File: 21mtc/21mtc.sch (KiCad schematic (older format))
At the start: 4 parts, among them P101 CONN_01X11, P102 CONN_02X11, P103 CONN_01X11, P104 CONN_02X04

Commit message: Layout of a first draft
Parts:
- removed P101: CONN_01X11, symbol CONN_01X10
- added P101: CONN_01X06, Connectors:solderpads_1x06_2mm, symbol CONN_01X06
- added P105: CONN_01X04, Connectors:solderpads_1x04_2mm, symbol CONN_01X04
- P102: footprint (none) -> Connectors:Pin_Header_Straight_2x11_1.27_smd
- P103: footprint (none) -> Connectors:solderpads_1x11_2mm
- P104: footprint (none) -> Pin_Headers:Pin_Header_Straight_2x04
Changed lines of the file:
@@
 F 0 "P102" H 4650 3800 50  0000 C CNN
 F 1 "CONN_02X11" V 4650 3200 50  0000 C CNN
-F 2 "" H 4650 2000 60  0000 C CNN
+F 2 "Connectors:Pin_Header_Straight_2x11_1.27_smd" H 4650 2000 60  0001 C CNN
 F 3 "" H 4650 2000 60  0000 C CNN
 	1    4650 3200
@@
 F 0 "P103" H 5400 2600 50  0000 C CNN
 F 1 "CONN_01X11" V 5500 3200 50  0000 C CNN
-F 2 "" H 5400 3200 60  0000 C CNN
+F 2 "Connectors:solderpads_1x11_2mm" H 5400 3200 60  0001 C CNN
 F 3 "" H 5400 3200 60  0000 C CNN
 F 4 "Value" H 5400 3200 60  0001 C CNN "Fieldname"
 	1    5400 3200
 	1    0    0    1
-$EndComp
-$Comp
-L CONN_01X10 P101
-U 1 1 566E68DE
-P 3900 3150
-F 0 "P101" H 3900 3700 50  0000 C CNN
-F 1 "CONN_01X11" V 4000 3150 50  0000 C CNN
-F 2 "" H 3900 3150 60  0000 C CNN
-F 3 "" H 3900 3150 60  0000 C CNN
-F 4 "Value" H 3900 3150 60  0001 C CNN "Fieldname"
-	1    3900 3150
-	-1   0    0    -1
 $EndComp
 Wire Wire Line
@@
 F 0 "P104" H 7100 3300 50  0000 C CNN
 F 1 "CONN_02X04" H 7100 2800 50  0000 C CNN
-F 2 "" H 7100 1850 60  0000 C CNN
+F 2 "Pin_Headers:Pin_Header_Straight_2x04" H 7100 1850 60  0001 C CNN
 F 3 "" H 7100 1850 60  0000 C CNN
 	1    7100 3050
@@
 Text Notes 7700 4000 2    60   ~ 0
 NEM 652 / NMRA Medium
+$Comp
+L CONN_01X06 P101
+U 1 1 566EB905
+P 3900 2950
+F 0 "P101" H 3900 3300 50  0000 C CNN
+F 1 "CONN_01X06" V 4000 2950 50  0000 C CNN
+F 2 "Connectors:solderpads_1x06_2mm" H 3900 2950 60  0001 C CNN
+F 3 "" H 3900 2950 60  0000 C CNN
+	1    3900 2950
+	-1   0    0    -1
+$EndComp
+$Comp
+L CONN_01X04 P105
+U 1 1 566EB947
+P 3900 3450
+F 0 "P105" H 3900 3200 50  0000 C CNN
+F 1 "CONN_01X04" V 4000 3450 50  0000 C CNN
+F 2 "Connectors:solderpads_1x04_2mm" H 3900 3450 60  0001 C CNN
+F 3 "" H 3900 3450 60  0000 C CNN
+	1    3900 3450
+	-1   0    0    -1
+$EndComp
 $EndSCHEMATC

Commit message: MTC21 Updates
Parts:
- added Q101: NTJD4401N, Housings_SOT-23_SOT-143_TSOT-6:SC-70-6_Handsoldering, symbol NTJD4401N
- added R101, R102, R103, R104: R, Resistors_SMD:R_0805_HandSoldering, symbol R
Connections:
- net GND: now also Q101.1 (S), Q101.4 (S), R101.2, R104.2
- net Aux3: no longer names the net of P103.2 (P2)
- net Aux3: now also Q101.3 (D); no longer P102.20 (P20)
- net Aux4: no longer names the net of P101.4 (P4)
- net Aux4: now also Q101.6 (D); no longer P102.7 (P7)
- new net: Q101.5 (G), R103.1, R104.1
- new net: Q101.2 (G), R101.1, R102.2
- new net Aux3_ttl: P102.20 (P20), R103.2
- new net Aux4_ttl: P102.7 (P7), R102.1
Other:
- moved on the sheet: P103
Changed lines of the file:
@@
 EESchema Schematic File Version 2
+LIBS:21mtc-rescue
 LIBS:power
 LIBS:device
@@
 LIBS:valves
 LIBS:21mtclogo
+LIBS:NTJD4401N
 LIBS:21mtc-cache
 EELAYER 25 0
@@
 L CONN_01X11 P103
 U 1 1 566E68B8
-P 5400 3200
-F 0 "P103" H 5400 2600 50  0000 C CNN
-F 1 "CONN_01X11" V 5500 3200 50  0000 C CNN
-F 2 "Connectors:solderpads_1x11_2mm" H 5400 3200 60  0001 C CNN
-F 3 "" H 5400 3200 60  0000 C CNN
-F 4 "Value" H 5400 3200 60  0001 C CNN "Fieldname"
-	1    5400 3200
+P 5800 3200
+F 0 "P103" H 5800 2600 50  0000 C CNN
+F 1 "CONN_01X11" V 5900 3200 50  0000 C CNN
+F 2 "Connectors:solderpads_1x11_2mm" H 5800 3200 60  0001 C CNN
+F 3 "" H 5800 3200 60  0000 C CNN
+F 4 "Value" H 5800 3200 60  0001 C CNN "Fieldname"
+	1    5800 3200
 	1    0    0    1
 $EndComp
@@
 	4100 2900 4400 2900
 Wire Wire Line
-	4100 3000 4400 3000
-Wire Wire Line
 	4100 3100 4400 3100
 Wire Wire Line
@@
 	4400 3600 4100 3600
 Wire Wire Line
-	4900 2700 5200 2700
-Wire Wire Line
-	5200 2800 4900 2800
-Wire Wire Line
-	4900 2900 5200 2900
-Wire Wire Line
-	5200 3000 4900 3000
-Wire Wire Line
-	4900 3100 5200 3100
-Wire Wire Line
-	4900 3200 5200 3200
-Wire Wire Line
-	5200 3300 4900 3300
-Wire Wire Line
-	4900 3400 5200 3400
-Wire Wire Line
-	5200 3500 4900 3500
-Wire Wire Line
-	4900 3600 5200 3600
-Wire Wire Line
-	5200 3700 4900 3700
+	4900 2700 5600 2700
+Wire Wire Line
+	4900 2800 5600 2800
+Wire Wire Line
+	4900 2900 5600 2900
+Wire Wire Line
+	4900 3000 5600 3000
+Wire Wire Line
+	4900 3100 5600 3100
+Wire Wire Line
+	4900 3200 5600 3200
+Wire Wire Line
+	4900 3300 5600 3300
+Wire Wire Line
+	4900 3400 5600 3400
+Wire Wire Line
+	4900 3500 5600 3500
+Wire Wire Line
+	4900 3700 5600 3700
 Text Label 4100 2700 0    60   ~ 0
 Hall1
@@
 Text Label 4100 2900 0    60   ~ 0
 Hall3
-Text Label 4100 3000 0    60   ~ 0
-Aux4
+Text Label 4400 3000 2    60   ~ 0
+Aux4_ttl
 Text Label 4100 3100 0    60   ~ 0
 TBClock
@@
 Vcc
 Text Label 4900 3600 0    60   ~ 0
-Aux3
+Aux3_ttl
 Text Label 4900 3500 0    60   ~ 0
 Aux2
@@
 L LOGO #G101
 U 1 1 566E6F08
-P 4650 4650
-F 0 "#G101" H 4650 4104 60  0001 C CNN
-F 1 "LOGO" H 4650 5196 60  0001 C CNN
-F 2 "" H 4650 4650 60  0000 C CNN
-F 3 "" H 4650 4650 60  0000 C CNN
-	1    4650 4650
-	1    0    0    -1
-$EndComp
-Text Notes 3900 4000 0    60   ~ 0
+P 4650 5100
+F 0 "#G101" H 4650 4554 60  0001 C CNN
+F 1 "LOGO" H 4650 5646 60  0001 C CNN
+F 2 "" H 4650 5100 60  0000 C CNN
+F 3 "" H 4650 5100 60  0000 C CNN
+	1    4650 5100
+	1    0    0    -1
+$EndComp
+Text Notes 3900 4450 0    60   ~ 0
 Tries to follow NMRA S9.1.1
 $Comp
@@
 	-1   0    0    -1
 $EndComp
+Wire Wire Line
+	4900 3600 5000 3600
+Wire Wire Line
+	4400 3000 4300 3000
+$Comp
+L NTJD4401N Q101
+U 2 1 56717E2C
+P 5400 4050
+F 0 "Q101" H 5600 4125 50  0000 L CNN
+F 1 "NTJD4401N" H 5600 4050 50  0000 L CNN
+F 2 "Housings_SOT-23_SOT-143_TSOT-6:SC-70-6_Handsoldering" H 5600 3975 50  0000 L CIN
+F 3 "" H 5400 4050 50  0000 L CNN
+	2    5400 4050
+	1    0    0    -1
+$EndComp
+$Comp
+L NTJD4401N Q101
+U 1 1 56717E59
+P 3600 4050
+F 0 "Q101" H 3800 4125 50  0000 L CNN
+F 1 "NTJD4401N" H 3800 4050 50  0000 L CNN
+F 2 "Housings_SOT-23_SOT-143_TSOT-6:SC-70-6_Handsoldering" H 3800 3975 50  0000 L CIN
+F 3 "" H 3600 4050 50  0000 L CNN
+	1    3600 4050
+	-1   0    0    -1
+$EndComp
+$Comp
+L R R103
+U 1 1 5673205A
+P 4950 4100
+F 0 "R103" V 5030 4100 50  0000 C CNN
+F 1 "R" V 4950 4100 50  0000 C CNN
+F 2 "Resistors_SMD:R_0805_HandSoldering" V 4880 4100 30  0001 C CNN
+F 3 "" H 4950 4100 30  0000 C CNN
+	1    4950 4100
+	0    1    1    0
+$EndComp
+$Comp
+L R R102
+U 1 1 5673208D
+P 4050 4100
+F 0 "R102" V 4130 4100 50  0000 C CNN
+F 1 "R" V 4050 4100 50  0000 C CNN
+F 2 "Resistors_SMD:R_0805_HandSoldering" V 3980 4100 30  0001 C CNN
+F 3 "" H 4050 4100 30  0000 C CNN
+	1    4050 4100
+	0    1    1    0
+$EndComp
+$Comp
+L R R101
+U 1 1 567320E9
+P 3850 4300
+F 0 "R101" V 3930 4300 50  0000 C CNN
+F 1 "R" V 3850 4300 50  0000 C CNN
+F 2 "Resistors_SMD:R_0805_HandSoldering" V 3780 4300 30  0001 C CNN
+F 3 "" H 3850 4300 30  0000 C CNN
+	1    3850 4300
+	1    0    0    -1
+$EndComp
+$Comp
+L R R104
+U 1 1 5673211C
+P 5150 4300
+F 0 "R104" V 5230 4300 50  0000 C CNN
+F 1 "R" V 5150 4300 50  0000 C CNN
+F 2 "Resistors_SMD:R_0805_HandSoldering" V 5080 4300 30  0001 C CNN
+F 3 "" H 5150 4300 30  0000 C CNN
+	1    5150 4300
+	1    0    0    -1
+$EndComp
+Wire Wire Line
+	5150 4150 5150 4100
+Wire Wire Line
+	5100 4100 5200 4100
+Connection ~ 5150 4100
+Wire Wire Line
+	3900 4100 3800 4100
+Wire Wire Line
+	3850 4150 3850 4100
+Connection ~ 3850 4100
+Wire Wire Line
+	4300 3000 4300 4100
+Wire Wire Line
+	4300 4100 4200 4100
+Wire Wire Line
+	5000 3600 5000 3850
+Wire Wire Line
+	5000 3850 4750 3850
+Wire Wire Line
+	4750 3850 4750 4100
+Wire Wire Line
+	4750 4100 4800 4100
+Wire Wire Line
+	5500 3850 5500 3600
+Wire Wire Line
+	5500 3600 5600 3600
+Wire Wire Line
+	3500 3850 4200 3850
+Wire Wire Line
+	4200 3850 4200 3000
+Wire Wire Line
+	4200 3000 4100 3000
+Wire Wire Line
+	3850 4450 3850 4500
+Wire Wire Line
+	3850 4500 3500 4500
+Wire Wire Line
+	3500 4250 3500 4600
+Wire Wire Line
+	5150 4450 5150 4500
+Wire Wire Line
+	5150 4500 5500 4500
+Wire Wire Line
+	5500 4250 5500 4600
+$Comp
+L GND #PWR01
+U 1 1 5673243C
+P 3500 4600
+F 0 "#PWR01" H 3500 4350 50  0001 C CNN
+F 1 "GND" H 3500 4450 50  0000 C CNN
+F 2 "" H 3500 4600 60  0000 C CNN
+F 3 "" H 3500 4600 60  0000 C CNN
+	1    3500 4600
+	1    0    0    -1
+$EndComp
+$Comp
+L GND #PWR02
+U 1 1 56732471
+P 5500 4600
+F 0 "#PWR02" H 5500 4350 50  0001 C CNN
+F 1 "GND" H 5500 4450 50  0000 C CNN
+F 2 "" H 5500 4600 60  0000 C CNN
+F 3 "" H 5500 4600 60  0000 C CNN
+	1    5500 4600
+	1    0    0    -1
+$EndComp
+$Comp
+L GND #PWR03
+U 1 1 567324A6
+P 5350 3800
+F 0 "#PWR03" H 5350 3550 50  0001 C CNN
+F 1 "GND" H 5350 3650 50  0000 C CNN
+F 2 "" H 5350 3800 60  0000 C CNN
+F 3 "" H 5350 3800 60  0000 C CNN
+	1    5350 3800
+	1    0    0    -1
+$EndComp
+Wire Wire Line
+	5350 3800 5350 2900
+Connection ~ 5350 2900
+Connection ~ 5500 4500
+Connection ~ 3500 4500
 $EndSCHEMATC

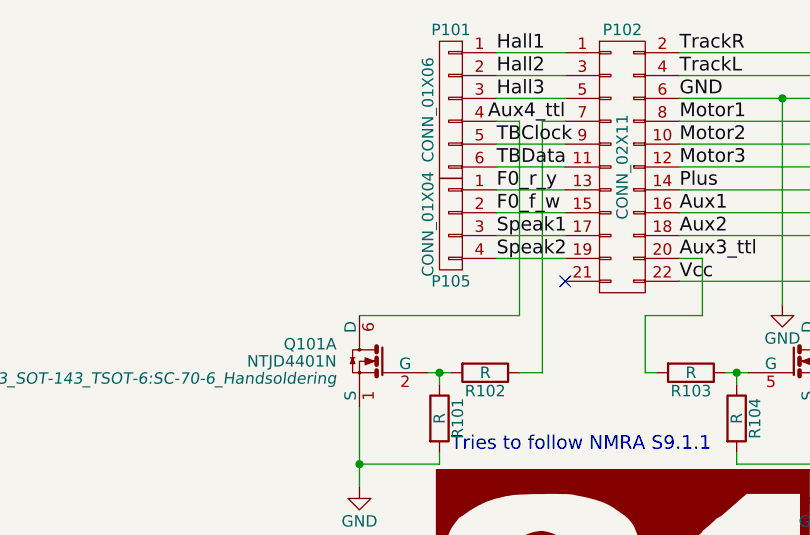
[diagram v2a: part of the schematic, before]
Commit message: Put the F0 pads on the front, moved the TB* pads to the back
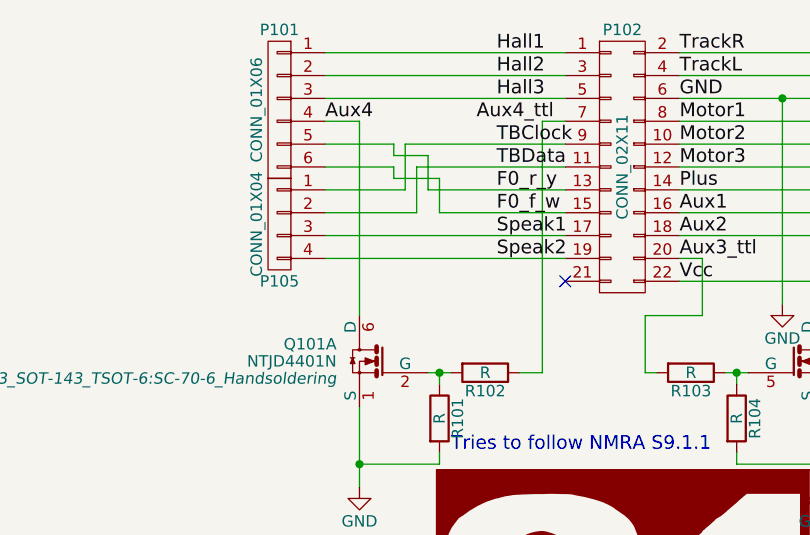
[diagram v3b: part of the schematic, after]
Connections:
- net F0_f_w: now also P101.6 (P6); no longer P105.2 (P2)
- net F0_r_y: now also P101.5 (P5); no longer P105.1 (P1)
- net TBClock: now also P105.1 (P1); no longer P101.5 (P5)
- net TBData: now also P105.2 (P2); no longer P101.6 (P6)
- net Aux4: now reaches P101.4 (P4), Q101.6 (D)
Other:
- moved on the sheet: P101, P105
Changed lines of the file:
@@
 EESchema Schematic File Version 2
-LIBS:21mtc-rescue
 LIBS:power
 LIBS:device
@@
 LIBS:valves
 LIBS:21mtclogo
-LIBS:NTJD4401N
 LIBS:21mtc-cache
 EELAYER 25 0
@@
 $EndComp
 Wire Wire Line
-	4100 2700 4400 2700
-Wire Wire Line
-	4400 2800 4100 2800
-Wire Wire Line
-	4100 2900 4400 2900
-Wire Wire Line
-	4100 3100 4400 3100
-Wire Wire Line
-	4400 3200 4100 3200
-Wire Wire Line
-	4100 3300 4400 3300
-Wire Wire Line
-	4400 3400 4100 3400
-Wire Wire Line
-	4100 3500 4400 3500
-Wire Wire Line
-	4400 3600 4100 3600
+	3350 2700 4400 2700
+Wire Wire Line
+	3350 2800 4400 2800
+Wire Wire Line
+	3350 2900 4400 2900
+Wire Wire Line
+	3800 3300 4400 3300
+Wire Wire Line
+	3850 3400 4400 3400
+Wire Wire Line
+	3350 3500 4400 3500
+Wire Wire Line
+	3350 3600 4400 3600
 Wire Wire Line
 	4900 2700 5600 2700
@@
 Text Label 4100 2900 0    60   ~ 0
 Hall3
-Text Label 4400 3000 2    60   ~ 0
+Text Label 4350 3000 2    60   ~ 0
 Aux4_ttl
 Text Label 4100 3100 0    60   ~ 0
@@
 L CONN_01X06 P101
 U 1 1 566EB905
-P 3900 2950
-F 0 "P101" H 3900 3300 50  0000 C CNN
-F 1 "CONN_01X06" V 4000 2950 50  0000 C CNN
-F 2 "Connectors:solderpads_1x06_2mm" H 3900 2950 60  0001 C CNN
-F 3 "" H 3900 2950 60  0000 C CNN
-	1    3900 2950
+P 3150 2950
+F 0 "P101" H 3150 3300 50  0000 C CNN
+F 1 "CONN_01X06" V 3250 2950 50  0000 C CNN
+F 2 "Connectors:solderpads_1x06_2mm" H 3150 2950 60  0001 C CNN
+F 3 "" H 3150 2950 60  0000 C CNN
+	1    3150 2950
 	-1   0    0    -1
 $EndComp
@@
 L CONN_01X04 P105
 U 1 1 566EB947
-P 3900 3450
-F 0 "P105" H 3900 3200 50  0000 C CNN
-F 1 "CONN_01X04" V 4000 3450 50  0000 C CNN
-F 2 "Connectors:solderpads_1x04_2mm" H 3900 3450 60  0001 C CNN
-F 3 "" H 3900 3450 60  0000 C CNN
-	1    3900 3450
+P 3150 3450
+F 0 "P105" H 3150 3200 50  0000 C CNN
+F 1 "CONN_01X04" V 3250 3450 50  0000 C CNN
+F 2 "Connectors:solderpads_1x04_2mm" H 3150 3450 60  0001 C CNN
+F 3 "" H 3150 3450 60  0000 C CNN
+	1    3150 3450
 	-1   0    0    -1
 $EndComp
@@
 Connection ~ 5150 4100
 Wire Wire Line
-	3900 4100 3800 4100
+	3800 4100 3900 4100
 Wire Wire Line
 	3850 4150 3850 4100
@@
 Wire Wire Line
 	5500 3600 5600 3600
-Wire Wire Line
-	3500 3850 4200 3850
-Wire Wire Line
-	4200 3850 4200 3000
-Wire Wire Line
-	4200 3000 4100 3000
 Wire Wire Line
 	3850 4450 3850 4500
@@
 Connection ~ 5500 4500
 Connection ~ 3500 4500
+Wire Wire Line
+	4400 3100 3700 3100
+Wire Wire Line
+	3700 3100 3700 3300
+Wire Wire Line
+	3700 3300 3350 3300
+Wire Wire Line
+	3350 3400 3750 3400
+Wire Wire Line
+	3750 3400 3750 3200
+Wire Wire Line
+	3750 3200 4400 3200
+Wire Wire Line
+	3350 3100 3650 3100
+Wire Wire Line
+	3650 3100 3650 3150
+Wire Wire Line
+	3650 3150 3800 3150
+Wire Wire Line
+	3800 3150 3800 3300
+Wire Wire Line
+	3850 3400 3850 3250
+Wire Wire Line
+	3850 3250 3650 3250
+Wire Wire Line
+	3650 3250 3650 3200
+Wire Wire Line
+	3650 3200 3350 3200
+Wire Wire Line
+	3500 3850 3500 3000
+Wire Wire Line
+	3500 3000 3350 3000
+Text Label 3350 3000 0    60   ~ 0
+Aux4
 $EndSCHEMATC

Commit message: Library management
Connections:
- net Motor1: now also P103.6 (P6); no longer P103.8 (P8)
- net Motor2: now also P103.5 (P5); no longer P103.7 (P7)
- net Plus: now also P101.4 (P4); no longer P103.5 (P5)
- net TrackL: now also P103.7 (P7); no longer P103.10 (P10)
- net TrackR: now also P103.8 (P8); no longer P103.11 (P11)
- net at Q101.3 (D): now also P103.10 (P10); no longer P103.2 (P2)
- net Aux4: no longer names the net of Q101.6 (D)
- net Aux4: now also P103.11 (P11); no longer P101.4 (P4)
- net Motor3 renamed Aux5
- net Aux5: now also P103.2 (P2); no longer P103.6 (P6)
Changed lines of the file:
@@
 	1    0    0    1
 $EndComp
-Wire Wire Line
-	3350 2700 4400 2700
-Wire Wire Line
-	3350 2800 4400 2800
-Wire Wire Line
-	3350 2900 4400 2900
-Wire Wire Line
-	3800 3300 4400 3300
-Wire Wire Line
-	3850 3400 4400 3400
-Wire Wire Line
-	3350 3500 4400 3500
-Wire Wire Line
-	3350 3600 4400 3600
-Wire Wire Line
-	4900 2700 5600 2700
-Wire Wire Line
-	4900 2800 5600 2800
-Wire Wire Line
-	4900 2900 5600 2900
-Wire Wire Line
-	4900 3000 5600 3000
-Wire Wire Line
-	4900 3100 5600 3100
-Wire Wire Line
-	4900 3200 5600 3200
-Wire Wire Line
-	4900 3300 5600 3300
-Wire Wire Line
-	4900 3400 5600 3400
-Wire Wire Line
-	4900 3500 5600 3500
-Wire Wire Line
-	4900 3700 5600 3700
 Text Label 4100 2700 0    60   ~ 0
 Hall1
@@
 Plus
 Text Label 4900 3200 0    60   ~ 0
-Motor3
+Aux5
 Text Label 4900 3100 0    60   ~ 0
 Motor2
@@
 	1    0    0    -1
 $EndComp
-Wire Wire Line
-	6850 2900 6350 2900
 Text Label 6350 2900 0    60   ~ 0
 Motor1
-Wire Wire Line
-	6850 3000 6350 3000
-Wire Wire Line
-	6850 3100 6350 3100
-Wire Wire Line
-	6850 3200 6350 3200
-Wire Wire Line
-	7350 2900 7850 2900
-Wire Wire Line
-	7350 3000 7850 3000
-Wire Wire Line
-	7350 3100 7850 3100
-Wire Wire Line
-	7350 3200 7850 3200
 Text Label 6350 3000 0    60   ~ 0
 F0_r_y
@@
 	-1   0    0    -1
 $EndComp
-Wire Wire Line
-	4900 3600 5000 3600
-Wire Wire Line
-	4400 3000 4300 3000
 $Comp
 L NTJD4401N Q101
@@
 F 1 "NTJD4401N" H 5600 4050 50  0000 L CNN
 F 2 "Housings_SOT-23_SOT-143_TSOT-6:SC-70-6_Handsoldering" H 5600 3975 50  0000 L CIN
-F 3 "" H 5400 4050 50  0000 L CNN
+F 3 "http://www.onsemi.com/pub/Collateral/NTJD4401N-D.PDF" H 5400 4050 50  0000 L CNN
 	2    5400 4050
 	1    0    0    -1
@@
 	1    0    0    -1
 $EndComp
-Wire Wire Line
-	5150 4150 5150 4100
-Wire Wire Line
-	5100 4100 5200 4100
-Connection ~ 5150 4100
-Wire Wire Line
-	3800 4100 3900 4100
-Wire Wire Line
-	3850 4150 3850 4100
-Connection ~ 3850 4100
-Wire Wire Line
-	4300 3000 4300 4100
-Wire Wire Line
-	4300 4100 4200 4100
-Wire Wire Line
-	5000 3600 5000 3850
-Wire Wire Line
-	5000 3850 4750 3850
-Wire Wire Line
-	4750 3850 4750 4100
-Wire Wire Line
-	4750 4100 4800 4100
-Wire Wire Line
-	5500 3850 5500 3600
-Wire Wire Line
-	5500 3600 5600 3600
-Wire Wire Line
-	3850 4450 3850 4500
-Wire Wire Line
-	3850 4500 3500 4500
-Wire Wire Line
-	3500 4250 3500 4600
-Wire Wire Line
-	5150 4450 5150 4500
-Wire Wire Line
-	5150 4500 5500 4500
-Wire Wire Line
-	5500 4250 5500 4600
 $Comp
 L GND #PWR01
@@
 	1    0    0    -1
 $EndComp
+Text Label 3350 3000 0    60   ~ 0
+Plus
+Wire Wire Line
+	3350 2700 4400 2700
+Wire Wire Line
+	3350 2800 4400 2800
+Wire Wire Line
+	3350 2900 4400 2900
+Wire Wire Line
+	3800 3300 4400 3300
+Wire Wire Line
+	3850 3400 4400 3400
+Wire Wire Line
+	3350 3500 4400 3500
+Wire Wire Line
+	3350 3600 4400 3600
+Wire Wire Line
+	4900 2900 5600 2900
+Wire Wire Line
+	4900 3400 5600 3400
+Wire Wire Line
+	4900 3500 5600 3500
+Wire Wire Line
+	6850 2900 6350 2900
+Wire Wire Line
+	6850 3000 6350 3000
+Wire Wire Line
+	6850 3100 6350 3100
+Wire Wire Line
+	6850 3200 6350 3200
+Wire Wire Line
+	7350 2900 7850 2900
+Wire Wire Line
+	7350 3000 7850 3000
+Wire Wire Line
+	7350 3100 7850 3100
+Wire Wire Line
+	7350 3200 7850 3200
+Wire Wire Line
+	4900 3600 5000 3600
+Wire Wire Line
+	4400 3000 4300 3000
+Wire Wire Line
+	5150 4150 5150 4100
+Wire Wire Line
+	5100 4100 5200 4100
+Connection ~ 5150 4100
+Wire Wire Line
+	3800 4100 3900 4100
+Wire Wire Line
+	3850 4150 3850 4100
+Connection ~ 3850 4100
+Wire Wire Line
+	4300 3000 4300 4100
+Wire Wire Line
+	4300 4100 4200 4100
+Wire Wire Line
+	5000 3600 5000 3850
+Wire Wire Line
+	5000 3850 4750 3850
+Wire Wire Line
+	4750 3850 4750 4100
+Wire Wire Line
+	4750 4100 4800 4100
+Wire Wire Line
+	5500 2800 5500 3850
+Wire Wire Line
+	3850 4450 3850 4500
+Wire Wire Line
+	3850 4500 3500 4500
+Wire Wire Line
+	3500 4250 3500 4600
+Wire Wire Line
+	5150 4450 5150 4500
+Wire Wire Line
+	5150 4500 5500 4500
+Wire Wire Line
+	5500 4250 5500 4600
 Wire Wire Line
 	5350 3800 5350 2900
@@
 	3650 3200 3350 3200
 Wire Wire Line
-	3500 3850 3500 3000
-Wire Wire Line
 	3500 3000 3350 3000
-Text Label 3350 3000 0    60   ~ 0
-Aux4
+Wire Wire Line
+	5500 2800 5600 2800
+Wire Wire Line
+	3500 3850 3500 3800
+Wire Wire Line
+	3500 3800 5450 3800
+Wire Wire Line
+	5450 3800 5450 2700
+Wire Wire Line
+	5450 2700 5600 2700
+Wire Wire Line
+	4900 2700 5400 2700
+Wire Wire Line
+	5400 2700 5400 3000
+Wire Wire Line
+	5400 3000 5600 3000
+Wire Wire Line
+	4900 2800 5300 2800
+Wire Wire Line
+	5300 2800 5300 3100
+Wire Wire Line
+	5300 3100 5600 3100
+Wire Wire Line
+	4900 3000 5250 3000
+Wire Wire Line
+	5250 3000 5250 3200
+Wire Wire Line
+	5250 3200 5600 3200
+Wire Wire Line
+	5600 3300 5200 3300
+Wire Wire Line
+	5200 3300 5200 3100
+Wire Wire Line
+	5200 3100 4900 3100
+Wire Wire Line
+	4900 3200 5150 3200
+Wire Wire Line
+	5150 3200 5150 3600
+Wire Wire Line
+	5150 3600 5600 3600
+Wire Wire Line
+	4900 3700 5600 3700
 $EndSCHEMATC
